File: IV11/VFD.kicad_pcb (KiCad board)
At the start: 2 copper layers, 225 x 80 mm, 71 parts, among them J1 USB_B, SW1 switch, SW2 switch, SW3 switch, SW4 switch, U1 74HC595, U10 UDN2981, U11 UDN2981, U12 UDN2981, U13 WeMos_mini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

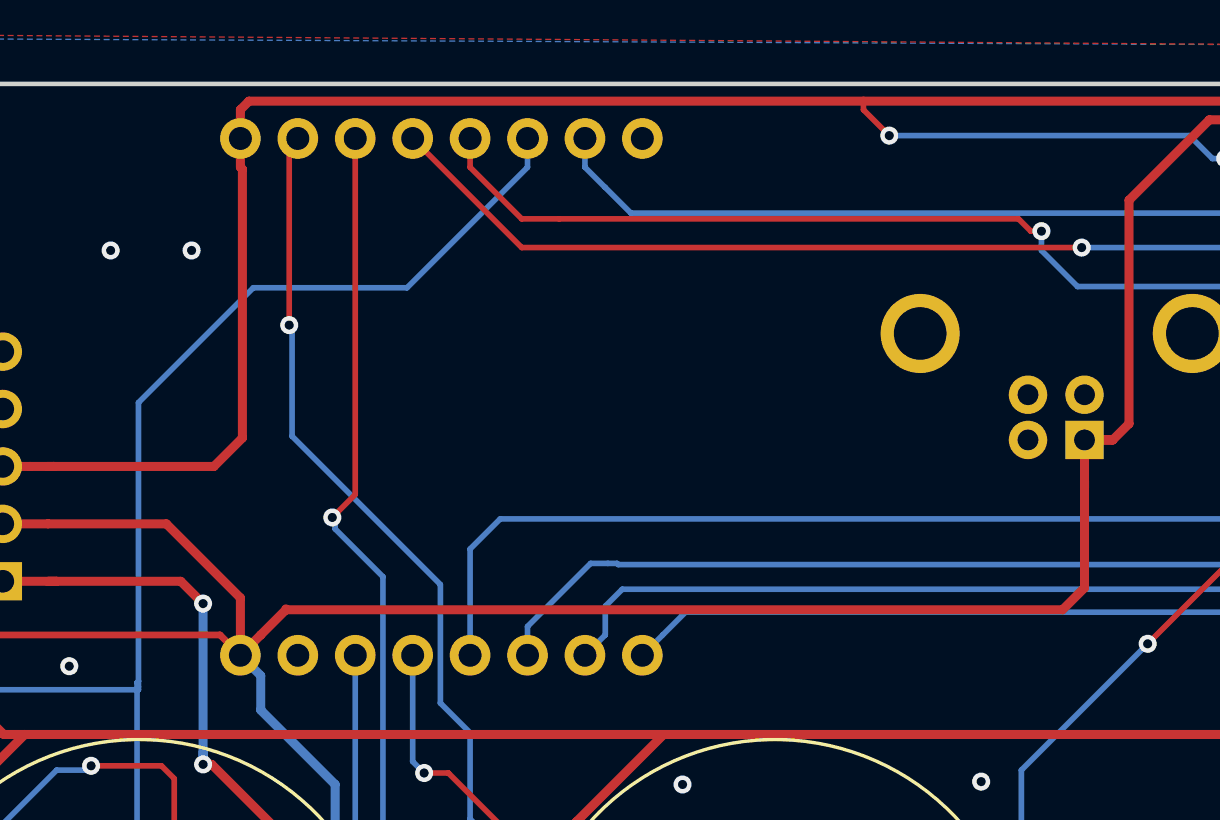
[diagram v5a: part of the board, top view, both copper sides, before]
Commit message: Fixes for not using D0 for the LEDs...
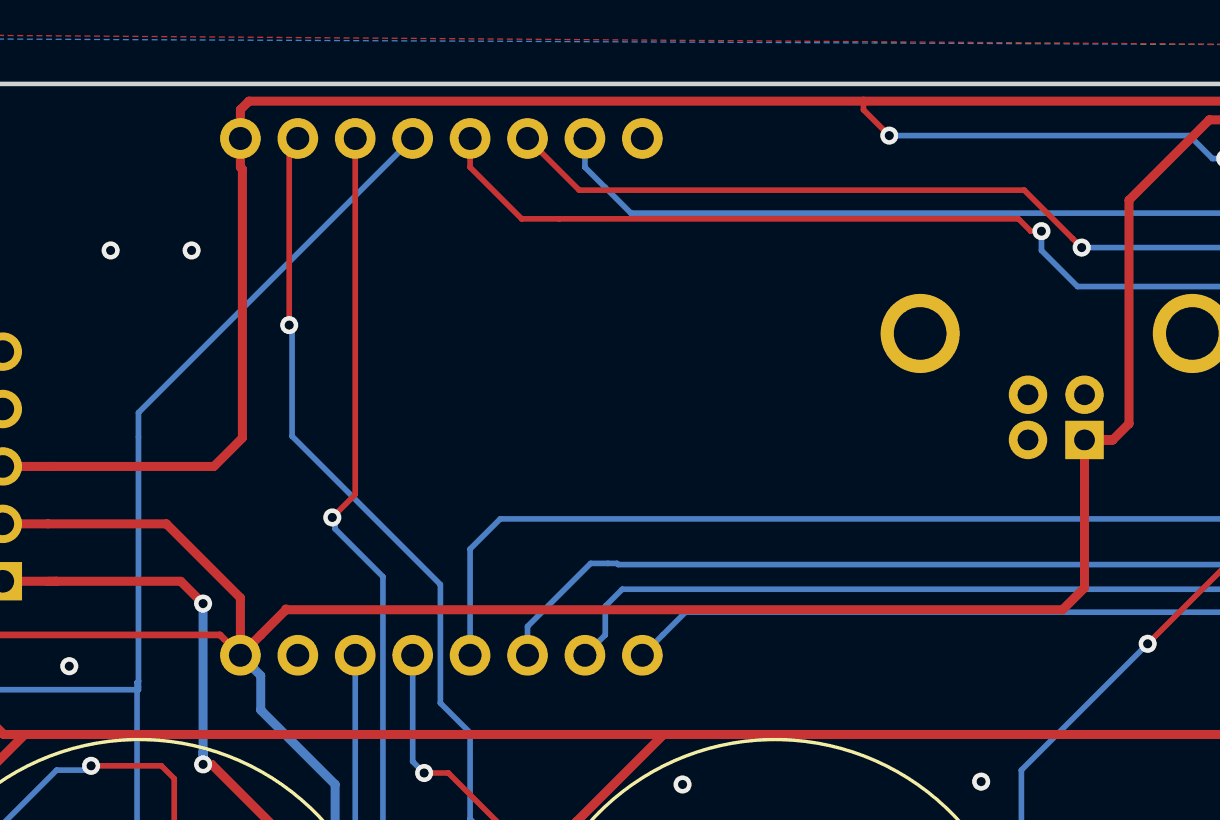
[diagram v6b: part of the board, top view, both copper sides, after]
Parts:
- R5: value 10k -> 100k
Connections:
- U13 pad 11: LED_DATA_IN -> SW_1
- U13 pad 13: SW_1 -> LED_DATA_IN
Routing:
- net LED_DATA_IN: track 91.7 -> 85.6 mm
- net SW_1: track 220.1 -> 215.2 mm
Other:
- board text added: "V1.1"
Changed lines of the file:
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@@
   (general
     (thickness 1.6)
-    (drawings 6)
+    (drawings 7)
     (tracks 2251)
     (zones 0)
@@
     (pad_to_mask_clearance 0.2)
     (aux_axis_origin 0 0)
-    (visible_elements FFFFF77F)
+    (visible_elements FFFFFF7F)
     (pcbplotparams
       (layerselection 0x010fc_ffffffff)
@@
       (net 24 SHIFT_OE))
     (pad 13 thru_hole circle (at 11.43 0 90) (size 1.8 1.8) (drill 1.016) (layers *.Cu *.Mask B.SilkS)
-      (net 26 SW_1))
+      (net 157 LED_DATA_IN))
     (pad 12 thru_hole circle (at 11.43 2.54 90) (size 1.8 1.8) (drill 1.016) (layers *.Cu *.Mask B.SilkS)
       (net 27 SW_2))
     (pad 11 thru_hole circle (at 11.43 5.08 90) (size 1.8 1.8) (drill 1.016) (layers *.Cu *.Mask B.SilkS)
-      (net 157 LED_DATA_IN))
+      (net 26 SW_1))
     (pad 10 thru_hole circle (at 11.43 7.62 90) (size 1.8 1.8) (drill 1.016) (layers *.Cu *.Mask B.SilkS)
       (net 156 LDR_IN))
@@
       (effects (font (size 1 1) (thickness 0.15)) (justify mirror))
     )
-    (fp_text value 10k (at 6.35 -2.92 180) (layer B.Fab)
+    (fp_text value 100k (at 6.35 -2.92 180) (layer B.Fab)
       (effects (font (size 1 1) (thickness 0.15)) (justify mirror))
     )
@@
       (net 158 SCL))
   )
+  (gr_text "V1.1\n" (at 29.718 15.24) (layer B.SilkS)
+    (effects (font (size 3 3) (thickness 0.3)) (justify mirror))
+  )
   (gr_text www.davidmpye.com/VFD (at 151.765 25.908) (layer B.SilkS)
     (effects (font (size 3 3) (thickness 0.3)) (justify mirror))
@@
   (segment (start 180.086 54.356) (end 180.721 54.991) (width 0.25) (layer B.Cu) (net 25))
   (segment (start 184.531 54.991) (end 185.42 55.88) (width 0.25) (layer B.Cu) (net 25))
-  (segment (start 26.162 2.413) (end 30.988 7.239) (width 0.25) (layer F.Cu) (net 26))
-  (segment (start 30.988 7.239) (end 55.499 7.239) (width 0.25) (layer F.Cu) (net 26))
   (via (at 55.753 7.239) (size 0.8) (drill 0.4) (layers F.Cu B.Cu) (net 26))
   (segment (start 55.499 7.239) (end 55.753 7.239) (width 0.25) (layer F.Cu) (net 26))
@@
   (segment (start 103.124 12.7) (end 103.124 16.002) (width 0.25) (layer F.Cu) (net 26))
   (segment (start 103.124 12.122685) (end 103.124 12.7) (width 0.25) (layer F.Cu) (net 26))
+  (segment (start 33.528 4.699) (end 53.213 4.699) (width 0.25) (layer F.Cu) (net 26))
+  (segment (start 55.353001 6.839001) (end 55.753 7.239) (width 0.25) (layer F.Cu) (net 26))
+  (segment (start 53.213 4.699) (end 55.353001 6.839001) (width 0.25) (layer F.Cu) (net 26))
+  (segment (start 31.242 2.413) (end 33.528 4.699) (width 0.25) (layer F.Cu) (net 26))
   (segment (start 28.702 3.685792) (end 30.985208 5.969) (width 0.25) (layer F.Cu) (net 27))
   (segment (start 28.702 2.413) (end 28.702 3.685792) (width 0.25) (layer F.Cu) (net 27))
@@
   (segment (start 97.409 12.065) (end 97.409 11.938) (width 0.25) (layer F.Cu) (net 156))
   (segment (start 97.409 11.938) (end 97.409 5.715) (width 0.25) (layer F.Cu) (net 156))
-  (segment (start 31.242 3.685792) (end 25.910792 9.017) (width 0.25) (layer B.Cu) (net 157))
-  (segment (start 31.242 2.413) (end 31.242 3.685792) (width 0.25) (layer B.Cu) (net 157))
-  (segment (start 25.910792 9.017) (end 19.1135 9.017) (width 0.25) (layer B.Cu) (net 157))
-  (segment (start 19.1135 9.017) (end 14.0335 14.097) (width 0.25) (layer B.Cu) (net 157))
   (segment (start 7.183001 55.689999) (end 3.873999 55.689999) (width 0.25) (layer F.Cu) (net 157))
   (segment (start 8.033 54.84) (end 7.183001 55.689999) (width 0.25) (layer F.Cu) (net 157))
@@
   (segment (start 13.97 26.4795) (end 14.0335 26.416) (width 0.25) (layer B.Cu) (net 157))
   (segment (start 13.97 36.783) (end 13.97 26.4795) (width 0.25) (layer B.Cu) (net 157))
-  (segment (start 14.0335 14.097) (end 14.0335 26.416) (width 0.25) (layer B.Cu) (net 157))
   (segment (start 14.0335 26.416) (end 14.0335 26.67) (width 0.25) (layer B.Cu) (net 157))
+  (segment (start 14.0335 14.5415) (end 14.0335 15.621) (width 0.25) (layer B.Cu) (net 157))
+  (segment (start 26.162 2.413) (end 14.0335 14.5415) (width 0.25) (layer B.Cu) (net 157))
+  (segment (start 14.0335 15.621) (end 14.0335 26.416) (width 0.25) (layer B.Cu) (net 157))
   (segment (start 159.852 13.174) (end 151.765 21.261) (width 0.25) (layer B.Cu) (net 158))
   (segment (start 160.252 13.174) (end 159.852 13.174) (width 0.25) (layer B.Cu) (net 158))
